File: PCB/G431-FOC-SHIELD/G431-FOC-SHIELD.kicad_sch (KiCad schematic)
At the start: 1 part

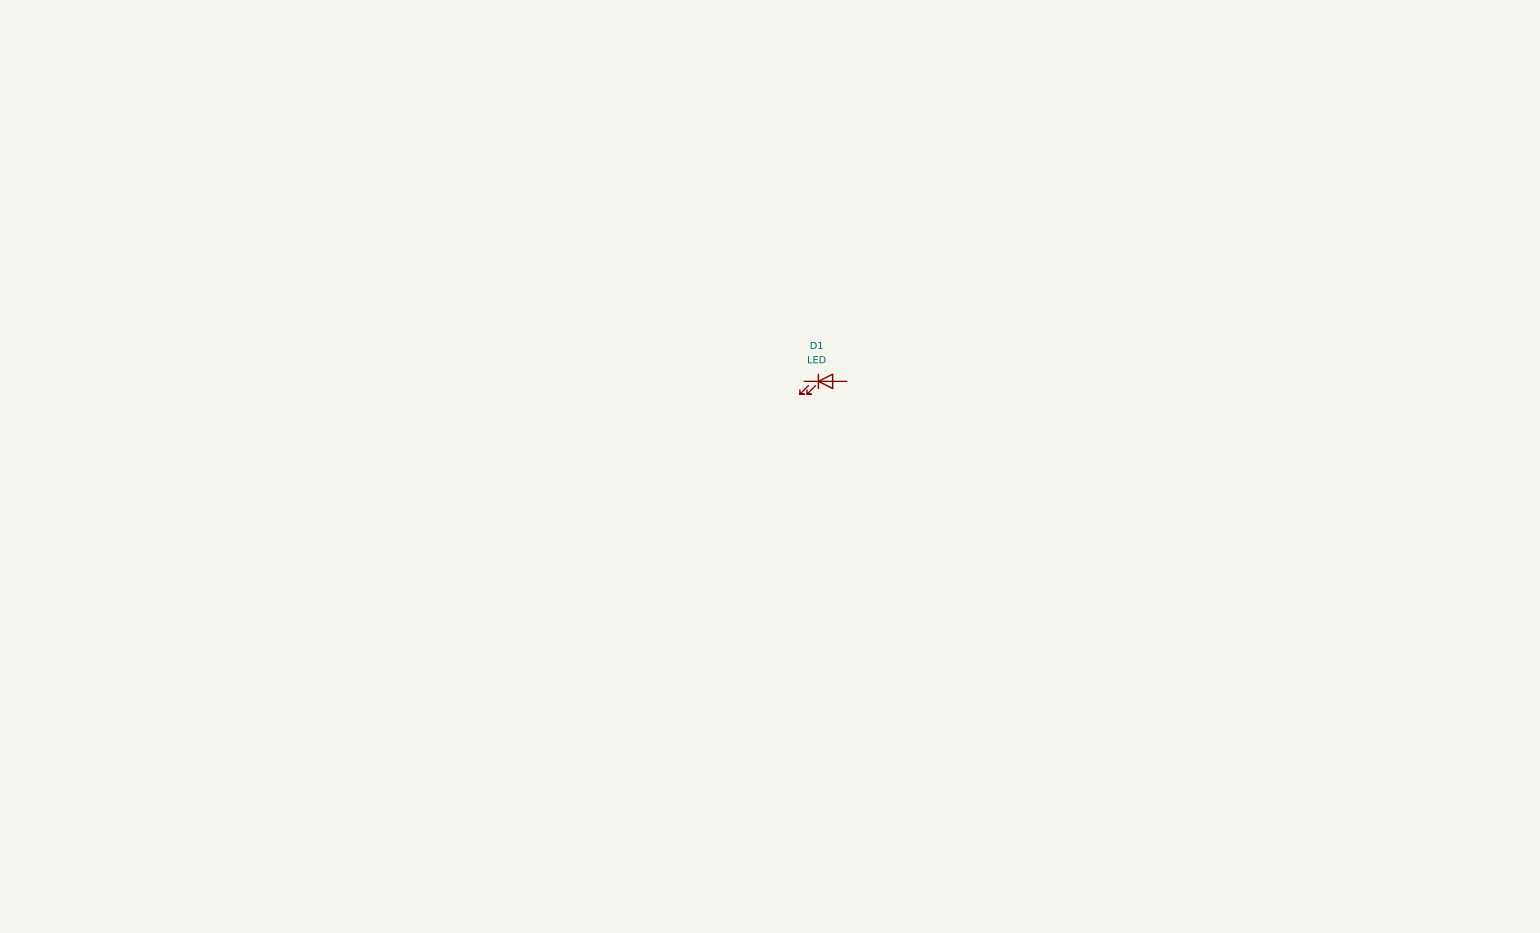
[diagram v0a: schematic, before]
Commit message: started schematic design, added DRV8323 typical application
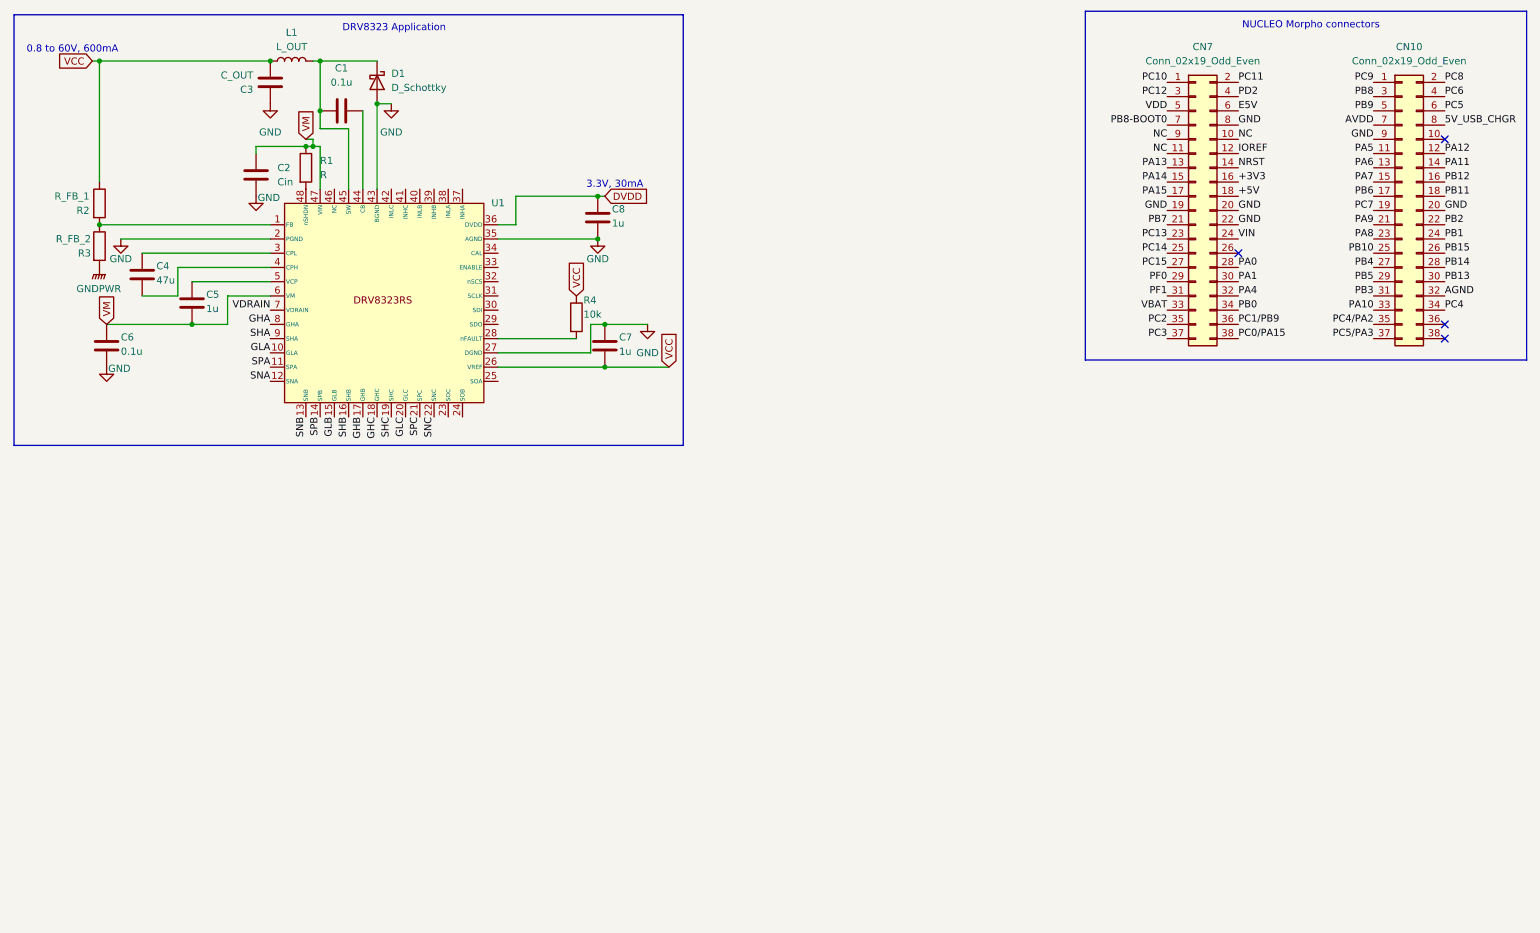
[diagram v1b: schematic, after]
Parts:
- removed D1: LED, LED_SMD:LED_0201_0603Metric, symbol Device:LED
- added C1, C6: 0.1u, Capacitor_SMD:C_0603_1608Metric, symbol Device:C
- added C2: Cin, Capacitor_SMD:C_0805_2012Metric, symbol Device:C
- added C3: C_OUT, Capacitor_SMD:C_0805_2012Metric, symbol Device:C
- added C4: 47u, Capacitor_SMD:C_0805_2012Metric, symbol Device:C
- added C5, C7, C8: 1u, Capacitor_SMD:C_0603_1608Metric, symbol Device:C
- added CN10, CN7: Conn_02x19_Odd_Even, Connector_PinSocket_2.54mm:PinSocket_2x19_P2.54mm_Vertical, symbol Connector_Generic:Conn_02x19_Odd_Even
- added D1: D_Schottky, Diode_SMD:D_SMA, symbol Device:D_Schottky
- added L1: L_OUT, Inductor_SMD:L_0805_2012Metric, symbol Device:L
- added R1: R, Resistor_SMD:R_0603_1608Metric, symbol Device:R
- added R2: R_FB_1, Resistor_SMD:R_0603_1608Metric, symbol Device:R
- added R3: R_FB_2, Resistor_SMD:R_0603_1608Metric, symbol Device:R
- added R4: 10k, Resistor_SMD:R_0603_1608Metric, symbol Device:R
- added U1: DRV8323RSRGZR, DRV8323RSRGZR:QFN50P700X700X100-49N, symbol DRV8323RSRGZR:DRV8323RSRGZR
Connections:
- new net: C1.1, D1.1 (K), L1.2, U1.45 (SW)
- new net: R2.2, R3.1, U1.1 (FB)
- new net: C4.1, U1.3 (CPL)
- new net: C4.2, U1.4 (CPH)
- new net: C5.1, U1.5 (VCP)
- new net: R4.2, U1.28 (nFAULT)
- new net: C1.2, U1.44 (CB)
- new net: R1.2, U1.48 (nSHDN)
- new net +3V3: CN7.16 (Pin_16)
- new net +5V: CN7.18 (Pin_18)
- new net 5V_USB_CHGR: CN10.8 (Pin_8)
- new net AGND: CN10.32 (Pin_32)
- new net AVDD: CN10.7 (Pin_7)
- new net DVDD: C8.1, U1.36 (DVDD)
- new net E5V: CN7.6 (Pin_6)
- new net GHA: U1.8 (GHA)
- new net GHB: U1.17 (GHB)
- new net GHC: U1.18 (GHC)
- new net GLA: U1.10 (GLA)
- new net GLB: U1.15 (GLB)
- new net GLC: U1.20 (GLC)
- new net GND: C2.2, C3.2, C6.2, C7.1, C8.2, CN10.20 (Pin_20), CN10.9 (Pin_9), CN7.19 (Pin_19), CN7.20 (Pin_20), CN7.22 (Pin_22), CN7.8 (Pin_8), D1.2 (A), U1.2 (PGND), U1.27 (DGND), U1.35 (AGND), U1.43 (BGND)
- new net GNDPWR: R3.2
- new net IOREF: CN7.12 (Pin_12)
- new net NC: CN7.10 (Pin_10), CN7.11 (Pin_11), CN7.9 (Pin_9)
- new net NRST: CN7.14 (Pin_14)
- new net PA0: CN7.28 (Pin_28)
- new net PA1: CN7.30 (Pin_30)
- new net PA10: CN10.33 (Pin_33)
- new net PA11: CN10.14 (Pin_14)
- new net PA12: CN10.12 (Pin_12)
- new net PA13: CN7.13 (Pin_13)
- new net PA14: CN7.15 (Pin_15)
- new net PA15: CN7.17 (Pin_17)
- new net PA4: CN7.32 (Pin_32)
- new net PA5: CN10.11 (Pin_11)
- new net PA6: CN10.13 (Pin_13)
- new net PA7: CN10.15 (Pin_15)
- new net PA8: CN10.23 (Pin_23)
- new net PA9: CN10.21 (Pin_21)
- new net PB0: CN7.34 (Pin_34)
- new net PB1: CN10.24 (Pin_24)
- new net PB10: CN10.25 (Pin_25)
- new net PB11: CN10.18 (Pin_18)
- new net PB12: CN10.16 (Pin_16)
- new net PB13: CN10.30 (Pin_30)
- new net PB14: CN10.28 (Pin_28)
- new net PB15: CN10.26 (Pin_26)
- new net PB2: CN10.22 (Pin_22)
- new net PB3: CN10.31 (Pin_31)
- new net PB4: CN10.27 (Pin_27)
- new net PB5: CN10.29 (Pin_29)
- new net PB6: CN10.17 (Pin_17)
- new net PB7: CN7.21 (Pin_21)
- new net PB8: CN10.3 (Pin_3)
- new net PB8-BOOT0: CN7.7 (Pin_7)
- new net PB9: CN10.5 (Pin_5)
- new net PC0/PA15: CN7.38 (Pin_38)
- new net PC10: CN7.1 (Pin_1)
- new net PC11: CN7.2 (Pin_2)
- new net PC12: CN7.3 (Pin_3)
- new net PC13: CN7.23 (Pin_23)
- new net PC14: CN7.25 (Pin_25)
- new net PC15: CN7.27 (Pin_27)
- new net PC1/PB9: CN7.36 (Pin_36)
- new net PC2: CN7.35 (Pin_35)
- new net PC3: CN7.37 (Pin_37)
- new net PC4: CN10.34 (Pin_34)
- new net PC4/PA2: CN10.35 (Pin_35)
- new net PC5: CN10.6 (Pin_6)
- new net PC5/PA3: CN10.37 (Pin_37)
- new net PC6: CN10.4 (Pin_4)
- new net PC7: CN10.19 (Pin_19)
- new net PC8: CN10.2 (Pin_2)
- new net PC9: CN10.1 (Pin_1)
- new net PD2: CN7.4 (Pin_4)
- new net PF0: CN7.29 (Pin_29)
- new net PF1: CN7.31 (Pin_31)
- new net SHA: U1.9 (SHA)
- new net SHB: U1.16 (SHB)
- new net SHC: U1.19 (SHC)
- new net SNA: U1.12 (SNA)
- new net SNB: U1.13 (SNB)
- new net SNC: U1.22 (SNC)
- new net SPA: U1.11 (SPA)
- new net SPB: U1.14 (SPB)
- new net SPC: U1.21 (SPC)
- new net VBAT: CN7.33 (Pin_33)
- new net VCC: C3.1, C7.2, L1.1, R2.1, R4.1, U1.26 (VREF)
- new net VDD: CN7.5 (Pin_5)
- new net VDRAIN: U1.7 (VDRAIN)
- new net VIN: CN7.24 (Pin_24)
- new net VM: C2.1, C5.2, C6.1, R1.1, U1.47 (VIN), U1.6 (VM)
- no-connect marks 0 -> 4
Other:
- note added: "0.8 to 60V, 600mA"
- note added: "3.3V, 30mA"
- note added: "DRV8323 Application"
- note added: "NUCLEO Morpho connectors"

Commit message: started calculations python script
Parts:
- added C9: C, Capacitor_SMD:C_0603_1608Metric, symbol Device:C
- added Q1, Q2: Q_NMOS, symbol Device:Q_NMOS
- added R5: R_SENSE, symbol Device:R
- C4: value 47u -> 47n
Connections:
- net SNA is gone; now on net GND: U1.12 (SNA)
- net GHA: now also Q1.G
- net GLA: now also Q2.G
- net GND: now also C9.2, R5.2
- net SPA: now also Q2.S, R5.1
- net VM: now also C9.1, Q1.D
- net SHA renamed A
- net A: now also Q1.S, Q2.D

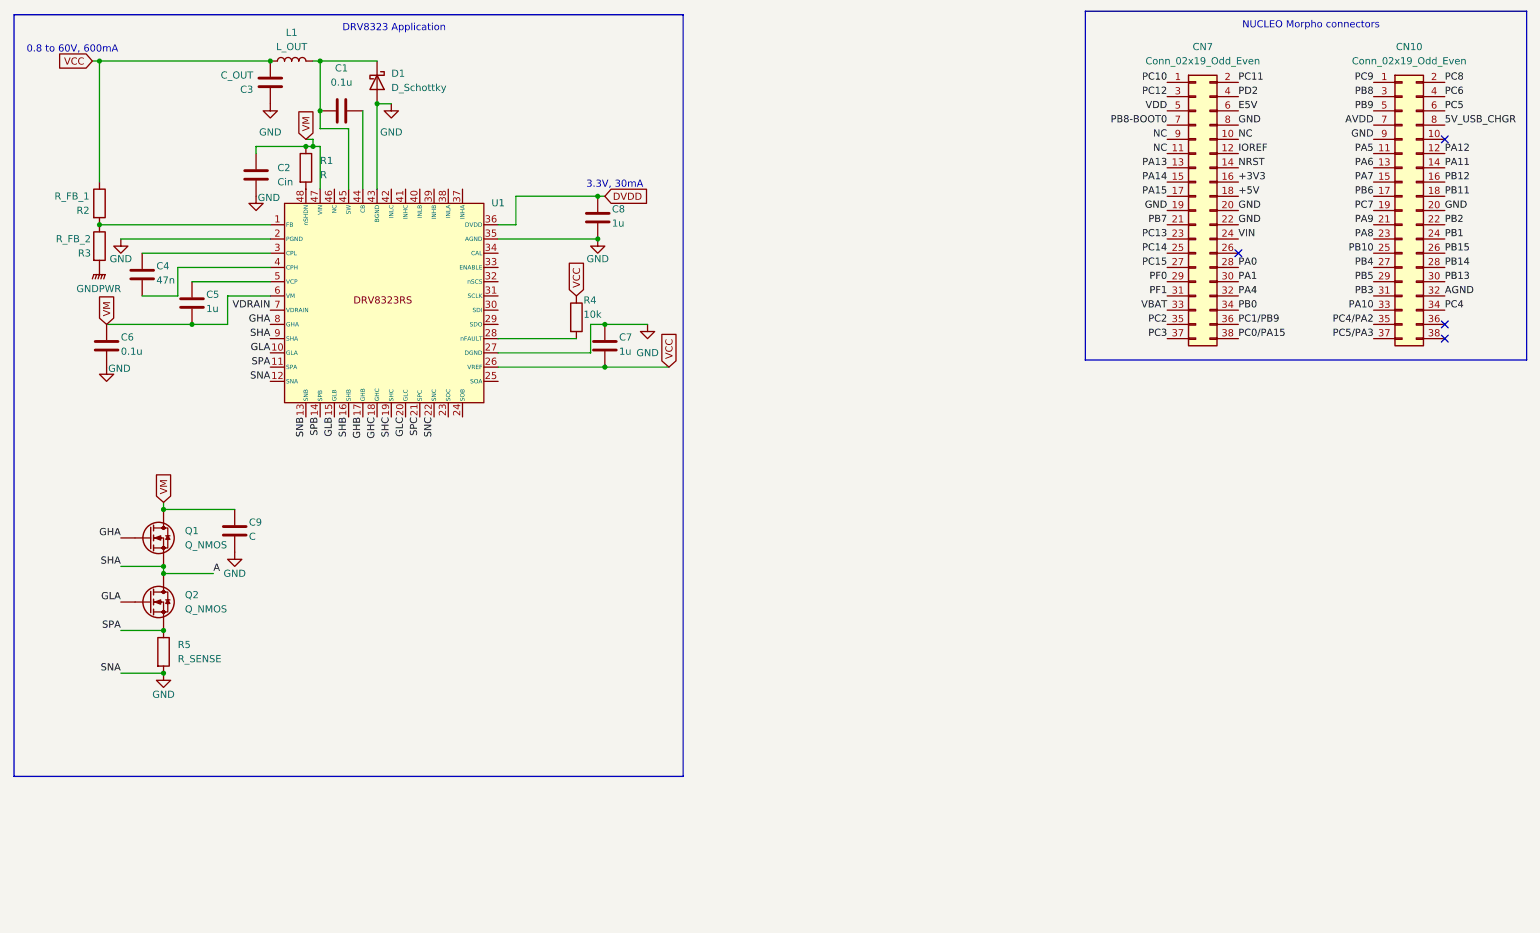
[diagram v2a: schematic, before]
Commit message: calculations in schematic
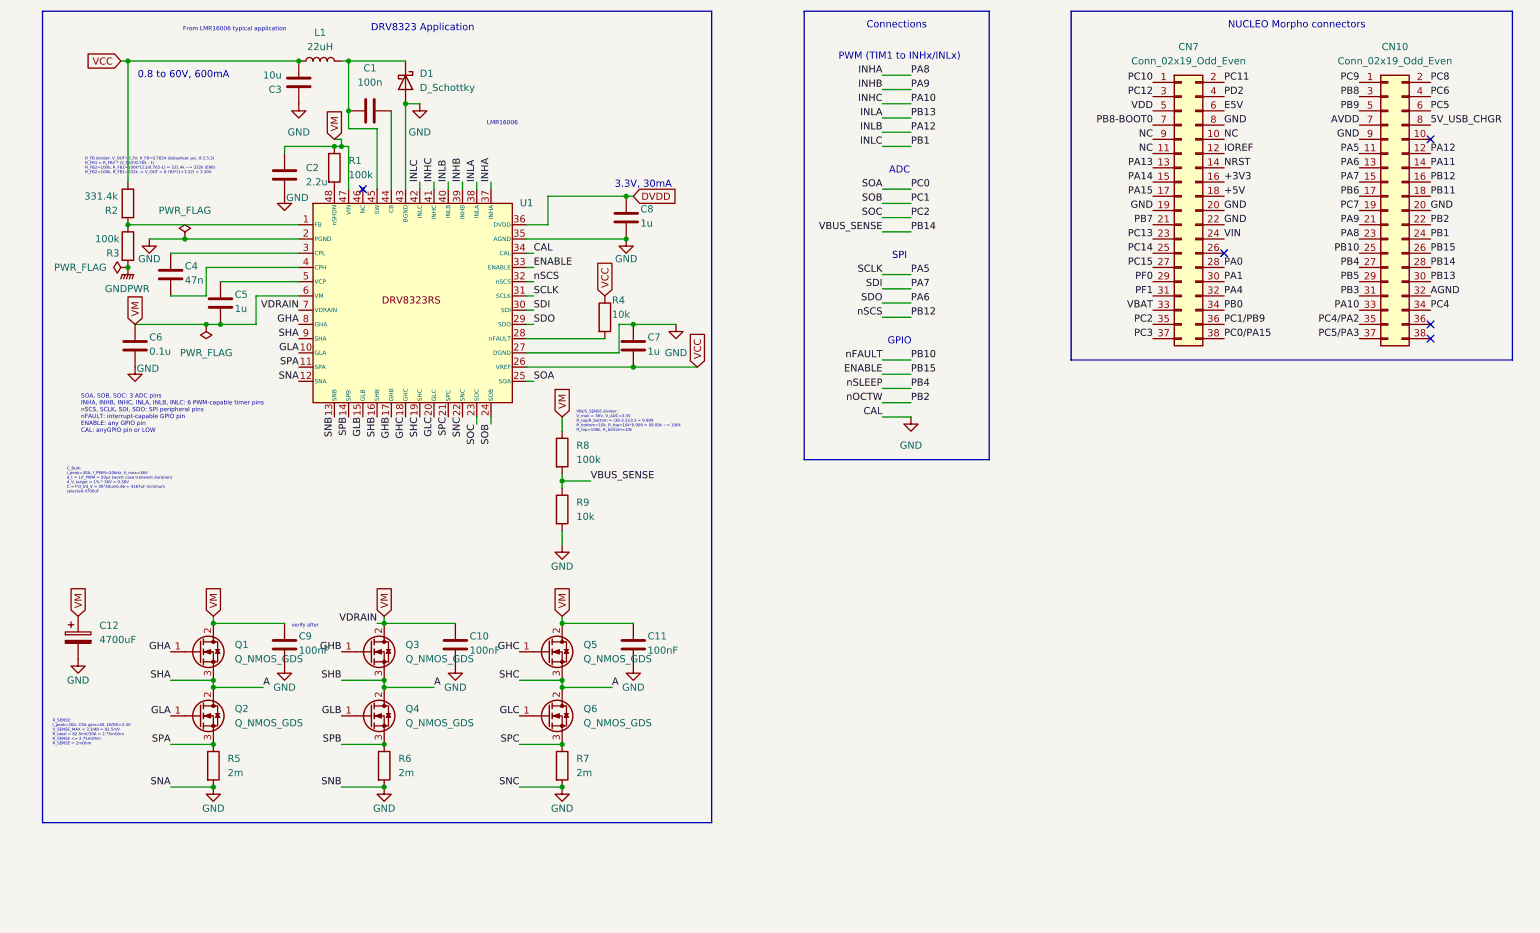
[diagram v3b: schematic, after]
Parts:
- removed Q1, Q2: Q_NMOS, symbol Device:Q_NMOS
- added C10, C11: 100nF, Capacitor_SMD:C_0603_1608Metric, symbol Device:C
- added C12: 4700uF, symbol Device:C_Polarized
- added Q1, Q2, Q3, Q4, Q5, Q6: Q_NMOS_GDS, symbol Transistor_FET:Q_NMOS_GDS
- added R6, R7: 2m, symbol Device:R
- added R8: 100k, symbol Device:R
- added R9: 10k, symbol Device:R
- C1: value 0.1u -> 100n
- C2: value Cin -> 2.2u
- C3: value C_OUT -> 10u
- C9: value C -> 100nF
- L1: value L_OUT -> 22uH; footprint Inductor_SMD:L_0805_2012Metric -> (none)
- R1: value R -> 100k
- R2: value R_FB_1 -> 331.4k
- R3: value R_FB_2 -> 100k
- R5: value R_SENSE -> 2m
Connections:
- net PA10 is gone; now on net INHC: CN10.33 (Pin_33)
- net PA12 is gone; now on net INLB: CN10.12 (Pin_12)
- net PA8 is gone; now on net INHA: CN10.23 (Pin_23)
- net PA9 is gone; now on net INHB: CN10.21 (Pin_21)
- net PB1 is gone; now on net INLC: CN10.24 (Pin_24)
- net PB13 is gone; now on net INLA: CN10.30 (Pin_30)
- net PB15 is gone; now on net ENABLE: CN10.26 (Pin_26)
- net SHB is gone; now on net A: U1.16 (SHB)
- net SHC is gone; now on net A: U1.19 (SHC)
- net SNB is gone; now on net GND: U1.13 (SNB)
- net SNC is gone; now on net GND: U1.22 (SNC)
- net VDRAIN is gone; now on net VM: U1.7 (VDRAIN)
- net A: now also Q1.3 (S), Q2.2 (D), Q3.3 (S), Q4.2 (D), Q5.3 (S), Q6.2 (D)
- net GHA: now also Q1.1 (G)
- net GHB: now also Q3.1 (G)
- net GHC: now also Q5.1 (G)
- net GLA: now also Q2.1 (G)
- net GLB: now also Q4.1 (G)
- net GLC: now also Q6.1 (G)
- net GND: now also U1.34 (CAL), C10.2, C11.2, C12.2, R6.2, R7.2, R9.2
- net PA5: now also U1.31 (SCLK)
- net PA6: now also U1.29 (SDO)
- net PA7: now also U1.30 (SDI)
- net PB12: now also U1.32 (nSCS)
- net PB14: now also R8.2, R9.1
- net PC2: now also U1.23 (SOC)
- net SPA: now also Q2.3 (S)
- net SPB: now also Q4.3 (S), R6.1
- net SPC: now also Q6.3 (S), R7.1
- net VM: now also C10.1, C11.1, C12.1, Q1.2 (D), Q3.2 (D), Q5.2 (D), R8.1
- net PC1: now reaches U1.24 (SOB)
- net PC0: now reaches U1.25 (SOA)
- net ENABLE: now reaches U1.33 (ENABLE)
- net INHA: now reaches U1.37 (INHA)
- net INLA: now reaches U1.38 (INLA)
- net INHB: now reaches U1.39 (INHB)
- net INLB: now reaches U1.40 (INLB)
- net INHC: now reaches U1.41 (INHC)
- net INLC: now reaches U1.42 (INLC)
- no-connect marks 4 -> 5
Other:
- note added: "ADC"
- note added: "C_Bulk: I_peak=30A, f_PWM=20kHz, V_max=36V d_t = 1/f_PWM = 50µs (worst case transient duration) d_V_target = 1% * 36V = 0.36V C = I*d_t/d_V = 30*50us/0.36 = 4167uF minimum selected 4700uF"
- note added: "Connections"
- note added: "From LMR16006 typical application"
- note added: "GPIO"
- note added: "LMR16006"
- note added: "PWM (TIM1 to INHx/INLx)"
- note added: "R_FB divider: V_OUT=3.3V, V_FB=0.765V (datasheet sec. 8.3.5.3) R_FB1 = R_FB2 * (V_OUT/0.765 - 1) R_FB2=100k, R_FB1=100k*(3.3/0.765-1) = 331.4k ~= 332k (E96) R_FB2=100k, R_FB1=332k -> V_OUT = 0.765*(1+3.32) = 3.30V"
- note added: "R_SENSE: I_peak=30A, CSA gain=40, DVDD=3.3V V_SENSE_MAX = 3.3/40 = 82.5mV R_ideal = 82.5mV/30A = 2.75mOhm R_SENSE <= 2.75mOhm R_SENSE = 2mOhm"
- note added: "SOA, SOB, SOC: 3 ADC pins INHA, INHB, INHC, INLA, INLB, INLC: 6 PWM-capable timer pins nSCS, SCLK, SDI, SDO: SPI peripheral pins nFAULT: interrupt-capable GPIO pin ENABLE: any GPIO pin CAL: anyGPIO pin or LOW"
- note added: "SPI"
- note added: "VBUS_SENSE divider: V_max = 36V, V_ADC=3.3V R_top/R_bottom = (36-3.3)/3.3 = 9.909 R_bottom=10k, R_top=10k*9.909 = 99.09k ~= 100k R_top=100k, R_bottom=10k"
- note added: "verify after"
- moved on the sheet: C1, C2, C3, C4, C5, C6, C7, C8, C9, CN10, CN7, D1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

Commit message: started layout
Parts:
- added J1: Screw_Terminal_01x02, TerminalBlock_Phoenix:TerminalBlock_Phoenix_MKDS-1,5-2_1x02_P5.00mm_Horizontal, symbol Connector:Screw_Terminal_01x02
- added J2: Screw_Terminal_01x03, TerminalBlock_Phoenix:TerminalBlock_Phoenix_MKDS-1,5-3_1x03_P5.00mm_Horizontal, symbol Connector:Screw_Terminal_01x03
- C10, C11, C9: value 100nF -> 4.7u; footprint Capacitor_SMD:C_0603_1608Metric -> Capacitor_SMD:C_1210_3225Metric
- C12: value 4700uF -> 4700u; footprint (none) -> Capacitor_THT:CP_Radial_D16.0mm_P7.50mm
- L1: footprint (none) -> Inductor_SMD:L_1210_3225Metric
- Q1, Q2, Q3, Q4, Q5, Q6: footprint (none) -> Package_TO_SOT_SMD:TO-263-3_TabPin2
- R5, R6, R7: footprint (none) -> Resistor_SMD:R_2512_6332Metric
- R8, R9: footprint (none) -> Resistor_SMD:R_0603_1608Metric
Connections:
- net A: now also J2.1 (Pin_1); no longer Q3.3 (S), Q4.2 (D), Q5.3 (S), Q6.2 (D), U1.16 (SHB), U1.19 (SHC)
- net GND: now also U1.49 (GND), J1.2 (Pin_2)
- net VM: now also J1.1 (Pin_1)
- new net B: J2.2 (Pin_2), Q3.3 (S), Q4.2 (D), U1.16 (SHB)
- new net C: J2.3 (Pin_3), Q5.3 (S), Q6.2 (D), U1.19 (SHC)
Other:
- moved on the sheet: C2
